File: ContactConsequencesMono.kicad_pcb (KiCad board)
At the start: 2 copper layers, 135 x 110 mm, 175 parts, among them IC1 TPD2E1B06, IC2 TPS73633, IC3 MCP73831/2-OT, IC4 TPS73618, IC5 MCP1640-SOT, J1 ISP, J10 Sense2, J11 I2C, J12 Serial, J13 I2S, J2 Line in, J3 Line out, J4 SD_Card, J5 USB_OTG, J6 Battery, J7 PWM, J8 IO, J9 Sense1, Q1 Q_PMOS_GSD, SW1 Reset, SW2 Charge select, SW3 sw_vol, SW4 Rotary_Encoder, SW5 sw_fadein, SW6 sw_fadeout, SW7 sw_touch, SW8 sw_mode, SW9 sw_release, U1 ATMEGA32U4-AU, U2 vs1053b, U3 MAX9723-TQFN, U4 MAX7219, U5 TCA9534, U6 TXS0108EPWR, Y1 16MHz, Y2 12,288MHz

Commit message: Board should be ok. Bargraph leds yet to do.
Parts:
- removed the R1 at (91.7, 105.3)
- removed the R3 at (97.0, 105.3)
- removed the R5 at (94.4, 105.3)
- added RN1: 500, Resistors_SMD:R_Array_Concave_4x0603, F.Cu at (138.1, 92.6)
- moved FID1 219.9 mm to (88.0, 138.0)
- moved D12 187.1 mm to (74.7, 182.8)
- moved D13 187.1 mm to (58.3, 187.5)
- moved D16 187.1 mm to (58.3, 192.2)
- moved D17 187.1 mm to (63.3, 187.5)
- moved D19 187.1 mm to (74.7, 178.2)
- moved D21 187.1 mm to (86.5, 168.5)
- moved D22 187.1 mm to (63.3, 192.2)
- moved D23 187.1 mm to (68.3, 187.5)
- moved D26 187.1 mm to (65.0, 173.5)
- moved D28 187.1 mm to (53.4, 188.2)
- moved D33 187.1 mm to (48.4, 188.2)
- moved D34 187.1 mm to (76.5, 168.5)
- moved D37 187.1 mm to (73.2, 192.1)
- moved D38 187.1 mm to (84.5, 177.8)
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- renumbered R2 to R1, R13 to R10, R14 to R11, R15 to R12, R16 to R13, R17 to R14, R18 to R15, R19 to R16, R20 to R17, R21 to R18, R22 to R19, R4 to R2, R23 to R20, R24 to R21, R25 to R22, R26 to R23, R27 to R24, R28 to R25, R29 to R26, R30 to R27, R31 to R28, R6 to R3, R7 to R4, R8 to R5, R9 to R6, R10 to R7, R11 to R8, R12 to R9, RN1 to RN2, RN2 to RN3
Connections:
- IC1 pad 2: /USB/DR- -> AGND
- IC1 pad 3: Net-(IC1-Pad3) -> /USB/DR-
- IC1 pad 4: AGND -> /USB/DR-
- IC1 pad 6: Net-(IC1-Pad6) -> /USB/DR+
- J7 pad 1: PWM1 -> PWM2
- J7 pad 2: PWM2 -> PWM1
- J7 pad 3: PWM3 -> PWM4
- J7 pad 4: PWM4 -> PWM3
- J7 pad 5: PWM5 -> PWM6
- J7 pad 6: PWM6 -> PWM5
- U5 pad 10: /Buttons/SW_6 -> /Buttons/SW_4
- U5 pad 11: /Buttons/ENC_A -> /Buttons/SW_5
- U5 pad 12: /Buttons/ENC_B -> /Buttons/SW_6
- U5 pad 4: /Buttons/SW_1 -> /Buttons/ENC_A
- U5 pad 5: /Buttons/SW_2 -> /Buttons/ENC_B
- U5 pad 6: /Buttons/SW_3 -> /Buttons/SW_1
- U5 pad 7: /Buttons/SW_4 -> /Buttons/SW_2
- U5 pad 9: /Buttons/SW_5 -> /Buttons/SW_3
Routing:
- net +5V: track 181.4 -> 318.9 mm, vias 3 -> 5
- net AGND: track 140.6 -> 248.9 mm, vias 14 -> 22
- net MISO: track 0.00 -> 83.8 mm, vias 0 -> 4
- net MOSI_L: track 0.00 -> 80.2 mm, vias 0 -> 4
- net CLK_L: track 0.00 -> 79.6 mm, vias 0 -> 4
- net DREQ: track 0.00 -> 71.4 mm, vias 0 -> 4
- net VS_MIDI_MODE: track 5.54 -> 76.4 mm, vias 0 -> 2
- net SDA_L: track 0.00 -> 61.9 mm, vias 0 -> 4
- net SCL_L: track 0.06 -> 59.7 mm, vias 0 -> 4
- net IO_INT: track 0.00 -> 59.1 mm, vias 0 -> 2
- net /Buttons/ENC_B: track 0.01 -> 55.8 mm, vias 0 -> 2
- net /Buttons/SW_6: track 0.00 -> 52.6 mm, vias 0 -> 2
- net /Buttons/ENC_A: track 0.00 -> 50.1 mm, vias 0 -> 2
- net VS_CS_L: track 0.00 -> 45.4 mm, vias 0 -> 2
- net Net-(R1-Pad2): track 3.29 -> 46.7 mm, vias 0 -> 1
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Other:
- outline, holes or cut-outs redrawn

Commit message: Seems to be good for fabrication launch. Probably minor things to fix.
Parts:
- removed D43: ST_01, LEDs:LED_0603
- removed D44: ST_00, LEDs:LED_0603
- added J7: Display - secondary, Connectors_perso:Hirose_FH12-16S-1_SH, B.Cu at (120.4, 165.8)
- added J8: Display - main, Connectors_perso:Hirose_FH12-16S-1_SH, F.Cu at (120.5, 137.9)
- D10: value VU_10 -> VU_05
- D11: value VU_09 -> VU_06
- D12: value VU_08 -> VU_07
- D13: value VU_07 -> VU_08
- D14: value VU_06 -> VU_09
- D15: value VU_05 -> VU_10
- D16: value VU_04 -> VU_11
- D17: value VU_03 -> VU_12
- D18: value VU_02 -> VU_13
- D19: value VU_01 -> VU_14
- D20: value VU_00 -> VU_15
- D21: value VU_31 -> VU_16
- D22: value VU_30 -> VU_17
- D23: value VU_29 -> VU_18
- D24: value VU_28 -> VU_19
- D25: value VU_27 -> VU_20
- D26: value VU_26 -> VU_21
- D27: value VU_25 -> VU_22
- D28: value VU_24 -> VU_23
- D29: value VU_23 -> VU_24
- D30: value VU_22 -> VU_25
- D31: value VU_21 -> VU_26
- D32: value VU_20 -> VU_27
- D33: value VU_19 -> VU_28
- D34: value VU_18 -> VU_29
- D35: value VU_17 -> VU_30
- D36: value VU_16 -> VU_31
- D37: value ST_07 -> ST_00
- D38: value ST_06 -> ST_01
- D39: value ST_05 -> ST_02
- D40: value ST_04 -> ST_03
- D41: value ST_03 -> ST_04
- D42: value ST_02 -> ST_05
- D5: value VU_15 -> VU_00
- D6: value VU_14 -> VU_01
- D7: value VU_13 -> VU_02
- D8: value VU_12 -> VU_03
- D9: value VU_11 -> VU_04
- moved D33 142.5 mm to (188.1, 159.8), turned to 270 degrees
- moved D36 141.9 mm to (194.9, 159.8), turned to 270 degrees
- moved D28 126.6 mm to (176.8, 159.8), turned to 270 degrees
- moved D29 125.0 mm to (179.0, 159.8), turned to 270 degrees
- moved D30 123.7 mm to (181.3, 159.8), turned to 270 degrees
- moved D35 121.3 mm to (192.6, 159.8), turned to 270 degrees
- moved D31 120.2 mm to (183.6, 159.8), turned to 270 degrees
- moved D32 116.7 mm to (185.8, 159.8), turned to 270 degrees
- moved D25 116.7 mm to (170.0, 159.8), turned to 270 degrees
- moved D27 116.2 mm to (174.5, 159.8), turned to 270 degrees
- moved D34 114.1 mm to (190.3, 159.8), turned to 270 degrees
- moved D42 114.1 mm to (194.8, 164.8)
- moved C46 113.8 mm to (131.4, 117.9), turned to 90 degrees
- moved D26 108.2 mm to (172.3, 159.8), turned to 270 degrees
- moved D41 106.4 mm to (180.8, 164.8)
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- renumbered J8 to J10, J9 to J11, J10 to J12, J11 to J13, J12 to J14, J13 to J15, J7 to J9
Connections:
- D10 pad 1: /Leds/DIG_1 -> /Leds/DIG_0
- D10 pad 2: /Leds/SEG_E -> /Leds/SEG_B
- D11 pad 1: /Leds/DIG_1 -> /Leds/DIG_0
- D11 pad 2: /Leds/SEG_F -> /Leds/SEG_A
- D12 pad 1: /Leds/DIG_1 -> /Leds/DIG_0
- D12 pad 2: /Leds/SEG_G -> /Leds/SEG_DP
- D13 pad 1: /Leds/DIG_0 -> /Leds/DIG_1
- D13 pad 2: /Leds/SEG_DP -> /Leds/SEG_G
- D14 pad 1: /Leds/DIG_0 -> /Leds/DIG_1
- D14 pad 2: /Leds/SEG_A -> /Leds/SEG_F
- D15 pad 1: /Leds/DIG_0 -> /Leds/DIG_1
- D15 pad 2: /Leds/SEG_B -> /Leds/SEG_E
- D16 pad 1: /Leds/DIG_0 -> /Leds/DIG_1
- D16 pad 2: /Leds/SEG_C -> /Leds/SEG_D
- D17 pad 1: /Leds/DIG_0 -> /Leds/DIG_1
- D17 pad 2: /Leds/SEG_D -> /Leds/SEG_C
- D18 pad 1: /Leds/DIG_0 -> /Leds/DIG_1
- D18 pad 2: /Leds/SEG_E -> /Leds/SEG_B
- D19 pad 1: /Leds/DIG_0 -> /Leds/DIG_1
- D19 pad 2: /Leds/SEG_F -> /Leds/SEG_A
- D20 pad 1: /Leds/DIG_0 -> /Leds/DIG_1
- D20 pad 2: /Leds/SEG_G -> /Leds/SEG_DP
- D21 pad 1: /Leds/DIG_3 -> /Leds/DIG_2
- D21 pad 2: /Leds/SEG_DP -> /Leds/SEG_G
- D22 pad 1: /Leds/DIG_3 -> /Leds/DIG_2
- D22 pad 2: /Leds/SEG_A -> /Leds/SEG_F
- D23 pad 1: /Leds/DIG_3 -> /Leds/DIG_2
- D23 pad 2: /Leds/SEG_B -> /Leds/SEG_E
- D24 pad 1: /Leds/DIG_3 -> /Leds/DIG_2
- D24 pad 2: /Leds/SEG_C -> /Leds/SEG_D
- D25 pad 1: /Leds/DIG_3 -> /Leds/DIG_2
- D25 pad 2: /Leds/SEG_D -> /Leds/SEG_C
- D26 pad 1: /Leds/DIG_3 -> /Leds/DIG_2
- D26 pad 2: /Leds/SEG_E -> /Leds/SEG_B
- D27 pad 1: /Leds/DIG_3 -> /Leds/DIG_2
- D27 pad 2: /Leds/SEG_F -> /Leds/SEG_A
- D28 pad 1: /Leds/DIG_3 -> /Leds/DIG_2
- D28 pad 2: /Leds/SEG_G -> /Leds/SEG_DP
- D29 pad 1: /Leds/DIG_2 -> /Leds/DIG_3
- D29 pad 2: /Leds/SEG_DP -> /Leds/SEG_G
- D30 pad 1: /Leds/DIG_2 -> /Leds/DIG_3
- D30 pad 2: /Leds/SEG_A -> /Leds/SEG_F
- D31 pad 1: /Leds/DIG_2 -> /Leds/DIG_3
- D31 pad 2: /Leds/SEG_B -> /Leds/SEG_E
- D32 pad 1: /Leds/DIG_2 -> /Leds/DIG_3
- D32 pad 2: /Leds/SEG_C -> /Leds/SEG_D
- D33 pad 1: /Leds/DIG_2 -> /Leds/DIG_3
- D33 pad 2: /Leds/SEG_D -> /Leds/SEG_C
- D34 pad 1: /Leds/DIG_2 -> /Leds/DIG_3
- D34 pad 2: /Leds/SEG_E -> /Leds/SEG_B
- D35 pad 1: /Leds/DIG_2 -> /Leds/DIG_3
- D35 pad 2: /Leds/SEG_F -> /Leds/SEG_A
- D36 pad 1: /Leds/DIG_2 -> /Leds/DIG_3
- D36 pad 2: /Leds/SEG_G -> /Leds/SEG_DP
- D37 pad 2: /Leds/SEG_DP -> /Leds/SEG_G
- D38 pad 2: /Leds/SEG_A -> /Leds/SEG_F
- D39 pad 2: /Leds/SEG_B -> /Leds/SEG_E
- D40 pad 2: /Leds/SEG_C -> /Leds/SEG_D
- D41 pad 2: /Leds/SEG_D -> /Leds/SEG_C
- D42 pad 2: /Leds/SEG_E -> /Leds/SEG_B
- D5 pad 1: /Leds/DIG_1 -> /Leds/DIG_0
- D5 pad 2: /Leds/SEG_DP -> /Leds/SEG_G
- D6 pad 1: /Leds/DIG_1 -> /Leds/DIG_0
- D6 pad 2: /Leds/SEG_A -> /Leds/SEG_F
- D7 pad 1: /Leds/DIG_1 -> /Leds/DIG_0
- D7 pad 2: /Leds/SEG_B -> /Leds/SEG_E
- D8 pad 1: /Leds/DIG_1 -> /Leds/DIG_0
- D8 pad 2: /Leds/SEG_C -> /Leds/SEG_D
- D9 pad 1: /Leds/DIG_1 -> /Leds/DIG_0
- D9 pad 2: /Leds/SEG_D -> /Leds/SEG_C
- J4 pad 10: Net-(J4-Pad10) -> (no net)
- J4 pad 11: Net-(J4-Pad11) -> (no net)
- J4 pad 8: Net-(J4-Pad8) -> (no net)
- J4 pad 9: Net-(J4-Pad9) -> (no net)
- J5 pad 4: Net-(J5-Pad4) -> (no net)
- J6 pad : (no net) -> AGND
- RN1 pad 2: Net-(RN1-Pad2) -> (no net)
- RN1 pad 7: Net-(RN1-Pad7) -> (no net)
- SW4 pad 4: (no net) -> AGND
- U2 pad 15: Net-(U2-Pad15) -> (no net)
- U2 pad 2: Net-(U2-Pad2) -> (no net)
- U2 pad 26: Net-(U2-Pad26) -> (no net)
- U2 pad 27: Net-(U2-Pad27) -> (no net)
- U2 pad 42: Net-(U2-Pad42) -> (no net)
- U4 pad 10: /Leds/DIG_5 -> (no net)
- U4 pad 24: Net-(U4-Pad24) -> (no net)
- U4 pad 5: /Leds/DIG_6 -> (no net)
- U4 pad 8: /Leds/DIG_7 -> (no net)
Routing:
- net /Leds/SEG_E: track 0.00 -> 118.7 mm, vias 0 -> 6
- net /Leds/SEG_G: track 0.00 -> 117.8 mm, vias 0 -> 6
- net /Leds/SEG_D: track 0.00 -> 115.2 mm, vias 0 -> 6
- net /Leds/SEG_F: track 0.00 -> 114.4 mm, vias 0 -> 4
- net /Leds/SEG_C: track 0.00 -> 107.6 mm, vias 0 -> 6
- net /Leds/DIG_3: track 0.00 -> 104.9 mm, vias 0 -> 11
- net /Leds/SEG_A: track 0.00 -> 104.3 mm, vias 0 -> 6
- net /Leds/SEG_B: track 0.00 -> 103.7 mm, vias 0 -> 4
- net /Leds/DIG_4: track 0.00 -> 102.5 mm, vias 0 -> 3
- net /Leds/SEG_DP: track 0.00 -> 101.4 mm, vias 0 -> 4
- net /Leds/DIG_2: track 0.00 -> 87.2 mm, vias 0 -> 11
- net AGND: track 248.9 -> 334.0 mm, vias 22 -> 34
- net /Leds/DIG_1: track 0.00 -> 73.3 mm, vias 0 -> 11
- net (no net): track 0.00 -> 65.5 mm
- net CLK: track 6.49 -> 69.3 mm, vias 0 -> 2
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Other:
- board size 135 x 110 mm -> 135 x 128 mm

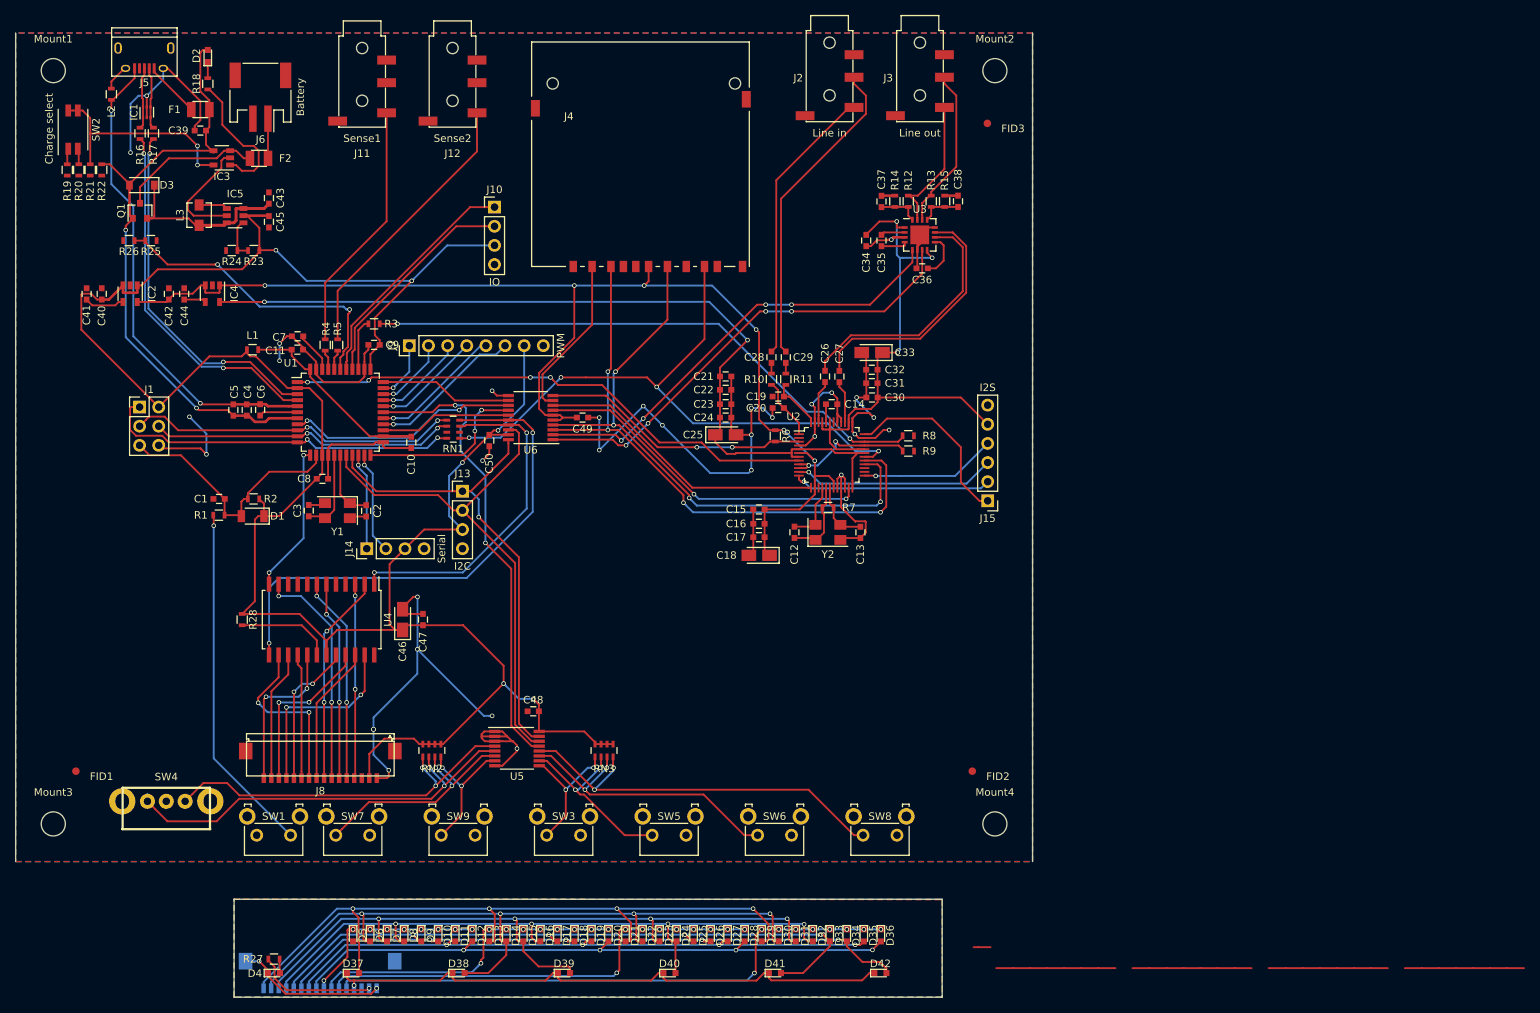
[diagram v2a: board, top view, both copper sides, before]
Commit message: Board modified after ckecking. Ready for fab, just need to create gerber, position and components files.
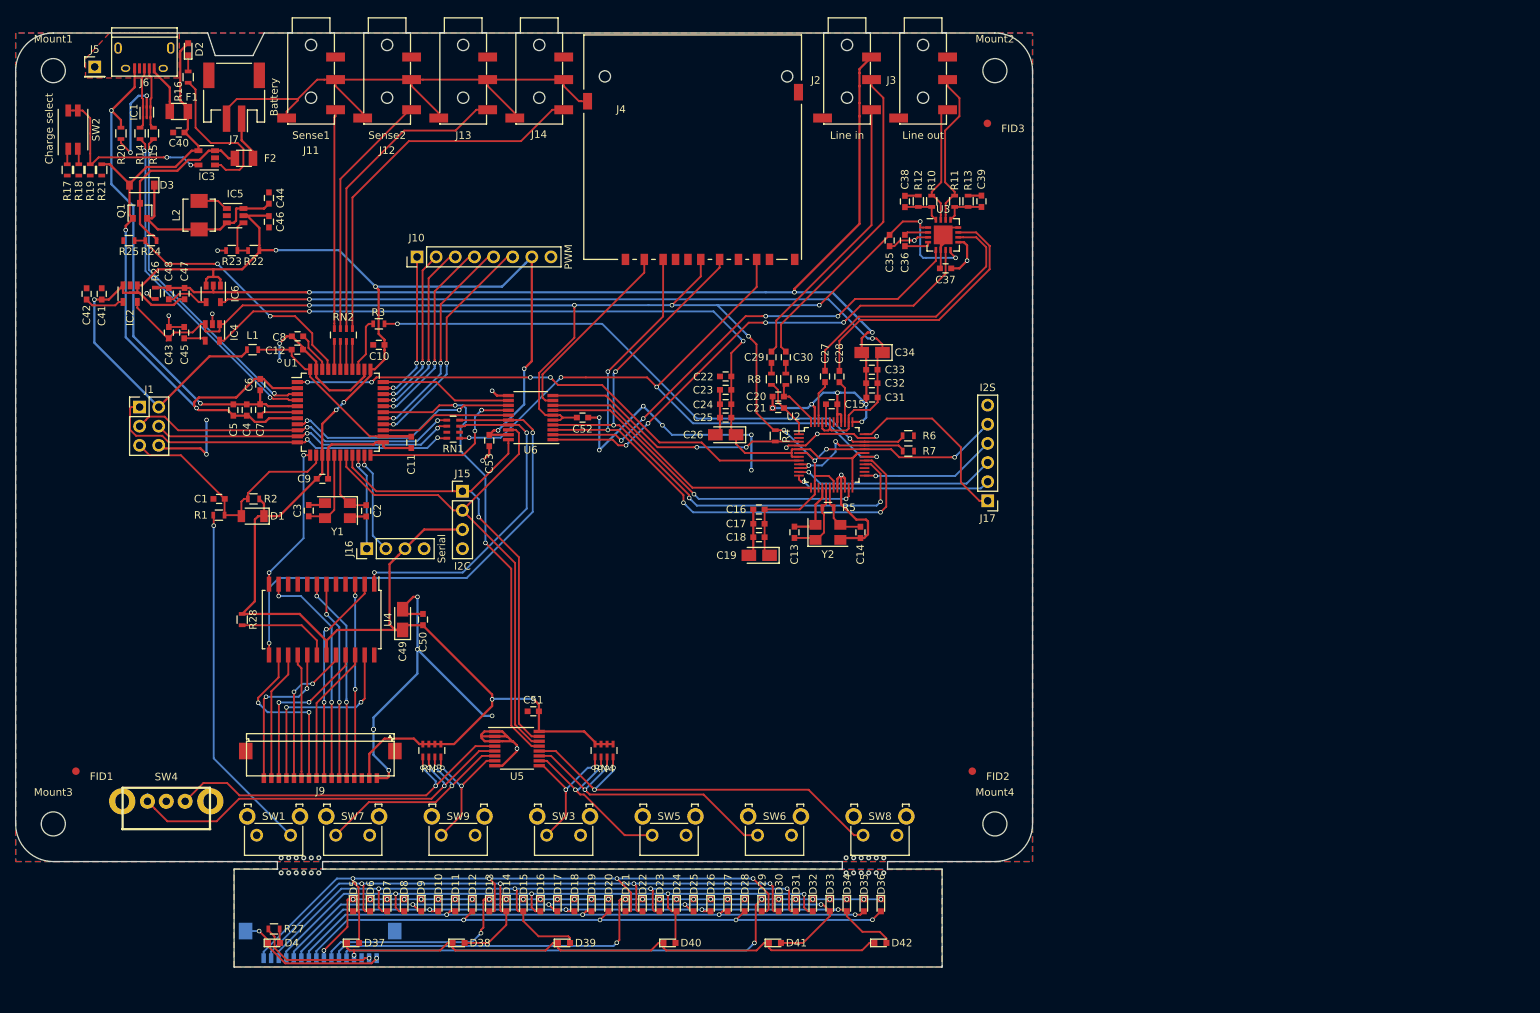
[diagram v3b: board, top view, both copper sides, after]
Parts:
- removed the J10 at (143.6, 63.1)
- removed L3: 4,7u, Inductors_SMD:L_Vishay_IHLP-1212
- removed the R4 at (121.1, 81.4)
- removed the R5 at (122.7, 81.4)
- added C47: 100n, Capacitors_SMD:C_0603, F.Cu at (102.4, 74.6)
- added C48: 10n, Capacitors_SMD:C_0603, F.Cu at (100.3, 74.6)
- added C6: 100n, Capacitors_SMD:C_0603, F.Cu at (112.5, 86.7)
- added IC6: TPS73633, TO_SOT_Packages_SMD:SOT-23-5, F.Cu at (106.2, 74.6)
- added J13: IO1, Connectors:PJ320D_3.5mm_Jack, F.Cu at (139.4, 46.4)
- added J14: IO2, Connectors:PJ320D_3.5mm_Jack, F.Cu at (149.5, 46.4)
- added J5: shield, Pin_Headers:Pin_Header_Straight_1x01_Pitch2.54mm, F.Cu at (90.5, 44.5)
- added R20: 0, Resistors_SMD:R_0603, F.Cu at (94.0, 53.3)
- added R26: 0, Resistors_SMD:R_0603, F.Cu at (98.6, 74.6)
- added RN2: 1k, Resistors_SMD:R_Array_Concave_4x0603, F.Cu at (123.5, 80.1)
- added S1: Mouse_bites_0.5_6, Holes_Fids:Mouse_bites_0.5_6, F.Cu at (117.8, 149.5)
- added S2: Mouse_bites_0.5_6, Holes_Fids:Mouse_bites_0.5_6, F.Cu at (117.8, 151.5)
- added S3: Mouse_bites_0.5_6, Holes_Fids:Mouse_bites_0.5_6, F.Cu at (192.8, 151.5)
- added S4: Mouse_bites_0.5_6, Holes_Fids:Mouse_bites_0.5_6, F.Cu at (192.8, 149.5)
- C52: renamed from C49; value C -> 100n
- C53: renamed from C50; value C -> 100n
- L1: value Ferrite_Bead -> 300
- L2: value Ferrite_Bead -> 4,7u; footprint Inductors_SMD:L_0603 -> Inductors_SMD:L_Vishay_IHLP-1616
- moved L2 19.8 mm to (104.4, 64.2), turned to 90 degrees
- moved J10 11.8 mm to (133.3, 69.7)
- moved J12 8.69 mm to (129.3, 46.4)
- moved J4 6.99 mm to (169.9, 57.9)
- moved J11 6.79 mm to (119.2, 46.4)
- moved C43 5.14 mm to (100.3, 79.8)
- moved C45 5.14 mm to (102.4, 79.8)
- moved IC4 5.14 mm to (106.1, 79.8)
- moved D10 4.00 mm to (136.1, 155.8)
- moved D11 4.00 mm to (138.4, 155.8)
- moved D12 4.00 mm to (140.6, 155.8)
- moved D13 4.00 mm to (142.9, 155.8)
- moved D14 4.00 mm to (145.1, 155.8)
- moved D15 4.00 mm to (147.4, 155.8)
- moved D16 4.00 mm to (149.7, 155.8)
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- renumbered C9 to C10, C10 to C11, C11 to C12, C12 to C13, C13 to C14, C14 to C15, C15 to C16, C16 to C17, C17 to C18, C18 to C19, C19 to C20, C20 to C21, C21 to C22, C22 to C23, C23 to C24, C24 to C25, C25 to C26, C26 to C27, C27 to C28, C28 to C29, C29 to C30, C30 to C31, C31 to C32, C32 to C33, C33 to C34, C34 to C35, C35 to C36, C36 to C37, C37 to C38, C38 to C39, C39 to C40, C40 to C41, C41 to C42, C42 to C43, C43 to C44, C44 to C45, C45 to C46, C46 to C49, C47 to C50, C48 to C51, C6 to C7, C7 to C8, C8 to C9, J9 to J10, J13 to J15, J14 to J16, J15 to J17, J5 to J6, J6 to J7, J7 to J8, J8 to J9, R12 to R10, R13 to R11, R14 to R12, R15 to R13, R16 to R14, R17 to R15, R18 to R16, R19 to R17, R20 to R18, R21 to R19, R22 to R21, R23 to R22, R24 to R23, R25 to R24, R26 to R25, R6 to R4, R7 to R5, R8 to R6, R9 to R7, R10 to R8, R11 to R9, RN2 to RN3, RN3 to RN4
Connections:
- C1 pad 2: AGND -> DGND
- C10 pad 2: AGND -> DGND
- C11 pad 1: AGND -> DGND
- C12 pad 2: AGND -> DGND
- C13 pad 2: AGND -> DGND
- C14 pad 2: AGND -> DGND
- C16 pad 2: AGND -> DGND
- C17 pad 2: AGND -> DGND
- C18 pad 2: AGND -> DGND
- C19 pad 2: AGND -> DGND
- C2 pad 2: AGND -> DGND
- C22 pad 2: AGND -> DGND
- C23 pad 2: AGND -> DGND
- C24 pad 2: AGND -> DGND
- C25 pad 2: AGND -> DGND
- C26 pad 2: AGND -> DGND
- C3 pad 2: AGND -> DGND
- C31 pad 1: +3V3 -> +3.3VA
- C32 pad 1: +3V3 -> +3.3VA
- C33 pad 1: +3V3 -> +3.3VA
- C34 pad 1: +3V3 -> +3.3VA
- C35 pad 1: AGND -> DGND
- C37 pad 2: AGND -> DGND
- C38 pad 1: AGND -> DGND
- C39 pad 1: AGND -> DGND
- C40 pad 2: AGND -> DGND
- C41 pad 2: AGND -> DGND
- C42 pad 2: AGND -> DGND
- C43 pad 2: AGND -> DGND
- C44 pad 1: Net-(C43-Pad1) -> Net-(C44-Pad1)
- C44 pad 2: AGND -> DGND
- C45 pad 2: AGND -> DGND
- C46 pad 2: AGND -> DGND
- C49 pad 2: AGND -> DGND
- C50 pad 2: AGND -> DGND
- C51 pad 1: AGND -> DGND
- C52 pad 2: AGND -> DGND
- C53 pad 1: AGND -> DGND
- C8 pad 1: AGND -> DGND
- C9 pad 1: AGND -> DGND
- D3 pad 1: Net-(C43-Pad1) -> Net-(C44-Pad1)
- D4 pad 1: AGND -> DGND
- IC1 pad 2: AGND -> DGND
- IC1 pad 5: AGND -> DGND
- IC2 pad 2: AGND -> DGND
- IC3 pad 2: AGND -> DGND
- IC4 pad 2: AGND -> DGND
- IC5 pad 2: AGND -> DGND
- IC5 pad 3: Net-(C43-Pad1) -> Net-(C44-Pad1)
- IC5 pad 6: Net-(C43-Pad1) -> Net-(C44-Pad1)
- J1 pad 6: AGND -> DGND
- J10 pad 8: AGND -> DGND
- J11 pad 2: AGND -> DGND
- J11 pad 3: (no net) -> DGND
- J11 pad 4: (no net) -> DGND
- J12 pad 2: AGND -> DGND
- J12 pad 3: (no net) -> DGND
- J12 pad 4: (no net) -> DGND
- J15 pad 4: AGND -> DGND
- J16 pad 4: AGND -> DGND
- J17 pad 6: AGND -> DGND
- J3 pad 3: AGND -> DGND
- J3 pad 4: (no net) -> DGND
- J4 pad 12: AGND -> DGND
- J4 pad 13: AGND -> DGND
- J4 pad 3: AGND -> DGND
- J4 pad 6: AGND -> DGND
- J6 pad 6: AGND -> Net-(J5-Pad1)
- J7 pad : AGND -> (no net)
- J7 pad 2: AGND -> DGND
- J8 pad 16: AGND -> DGND
- J8 pad 17: AGND -> DGND
- J9 pad 1: AGND -> DGND
- J9 pad 17: AGND -> DGND
- L2 pad 1: AGND -> Net-(C44-Pad1)
- L2 pad 2: UGND -> Net-(IC5-Pad1)
- Q1 pad 2: Net-(C43-Pad1) -> Net-(C44-Pad1)
- R12 pad 1: AGND -> DGND
- R13 pad 1: AGND -> DGND
- R17 pad 2: AGND -> DGND
- R18 pad 2: AGND -> DGND
- R19 pad 2: AGND -> DGND
- R21 pad 2: AGND -> DGND
- R23 pad 2: AGND -> DGND
- R25 pad 2: AGND -> DGND
- R6 pad 2: AGND -> DGND
- R7 pad 2: AGND -> DGND
- SW1 pad : (no net) -> DGND
- SW1 pad 2: AGND -> DGND
- SW3 pad : (no net) -> DGND
- SW3 pad 1: AGND -> DGND
- SW4 pad 2: AGND -> DGND
- SW4 pad 4: AGND -> DGND
- SW5 pad : (no net) -> DGND
- SW5 pad 1: AGND -> DGND
- SW6 pad : (no net) -> DGND
- SW6 pad 1: AGND -> DGND
- SW7 pad : (no net) -> DGND
- SW7 pad 1: AGND -> DGND
- SW8 pad : (no net) -> DGND
- SW8 pad 1: AGND -> DGND
- SW9 pad : (no net) -> DGND
- SW9 pad 1: AGND -> DGND
- U1 pad 15: AGND -> DGND
- U1 pad 2: +5V -> VBUS
- U1 pad 23: AGND -> DGND
- U1 pad 35: AGND -> DGND
- U1 pad 37: IO2 -> Net-(RN2-Pad4)
- U1 pad 38: IO1 -> Net-(RN2-Pad3)
- U1 pad 39: BATT_LEVEL -> Net-(RN2-Pad2)
- U1 pad 41: Net-(R4-Pad2) -> BATT_LEVEL
- U1 pad 43: AGND -> DGND
- U2 pad 16: AGND -> DGND
- U2 pad 20: AGND -> DGND
- U2 pad 21: AGND -> DGND
- U2 pad 22: AGND -> DGND
- U2 pad 35: AGND -> DGND
- U2 pad 38: +3V3 -> +3.3VA
- U2 pad 4: AGND -> DGND
- U2 pad 43: +3V3 -> +3.3VA
- U2 pad 45: +3V3 -> +3.3VA
- U3 pad 3: AGND -> DGND
- U3 pad 9: AGND -> DGND
- U4 pad 4: AGND -> DGND
- U4 pad 9: AGND -> DGND
- U5 pad 1: AGND -> DGND
- U5 pad 2: AGND -> DGND
- U5 pad 3: AGND -> DGND
- U5 pad 8: AGND -> DGND
- U6 pad 11: AGND -> DGND
- Y1 pad 2: AGND -> DGND
- Y1 pad 4: AGND -> DGND
- Y2 pad 2: AGND -> DGND
- Y2 pad 4: AGND -> DGND
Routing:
- net DGND: track 0.00 -> 342.5 mm, vias 0 -> 33
- net AGND: track 334.0 -> 172.0 mm, vias 34 -> 8
- net +3.3VA: track 0.00 -> 110.7 mm, vias 0 -> 2
- net (no net): track 65.5 -> 0.00 mm
- net IO_2: track 0.00 -> 50.3 mm
- net IO_1: track 0.00 -> 41.7 mm
- net IO1: track 31.6 -> 0.00 mm
- net IO2: track 29.8 -> 0.00 mm
- net Net-(C43-Pad1): track 24.4 -> 0.00 mm
- net Net-(C44-Pad1): track 0.00 -> 24.3 mm
- net VBUS: track 81.9 -> 97.0 mm
- net PWM2: track 7.82 -> 20.3 mm, vias 1 -> 2
- net PWM1: track 9.94 -> 22.1 mm, vias 1 -> 2
- net PWM4: track 12.2 -> 24.4 mm, vias 1 -> 2
- net PWM3: track 14.4 -> 26.3 mm, vias 1 -> 2
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- added copper zone on B.Cu, net DGND
- added copper zone on F.Cu, net DGND
- added copper zone on F.Cu, net Net-(J5-Pad1)
- removed copper zone on B.Cu, net AGND
- removed copper zone on F.Cu, net AGND
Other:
- board size 135 x 128 mm -> 135 x 124 mm
- net class AGND added: clearance 0.2, trace_width 0.3, via_dia 0.6, via_drill 0.4
- net class Power: trace_width 0.25 -> 0.3
- net class Sense: clearance 0.8 -> 0.4
- board text added: "Bluetooth HC03 module (one day)"
